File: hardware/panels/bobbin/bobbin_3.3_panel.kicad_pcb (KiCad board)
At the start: 2 copper layers, 68.5 x 105 mm, 34 parts

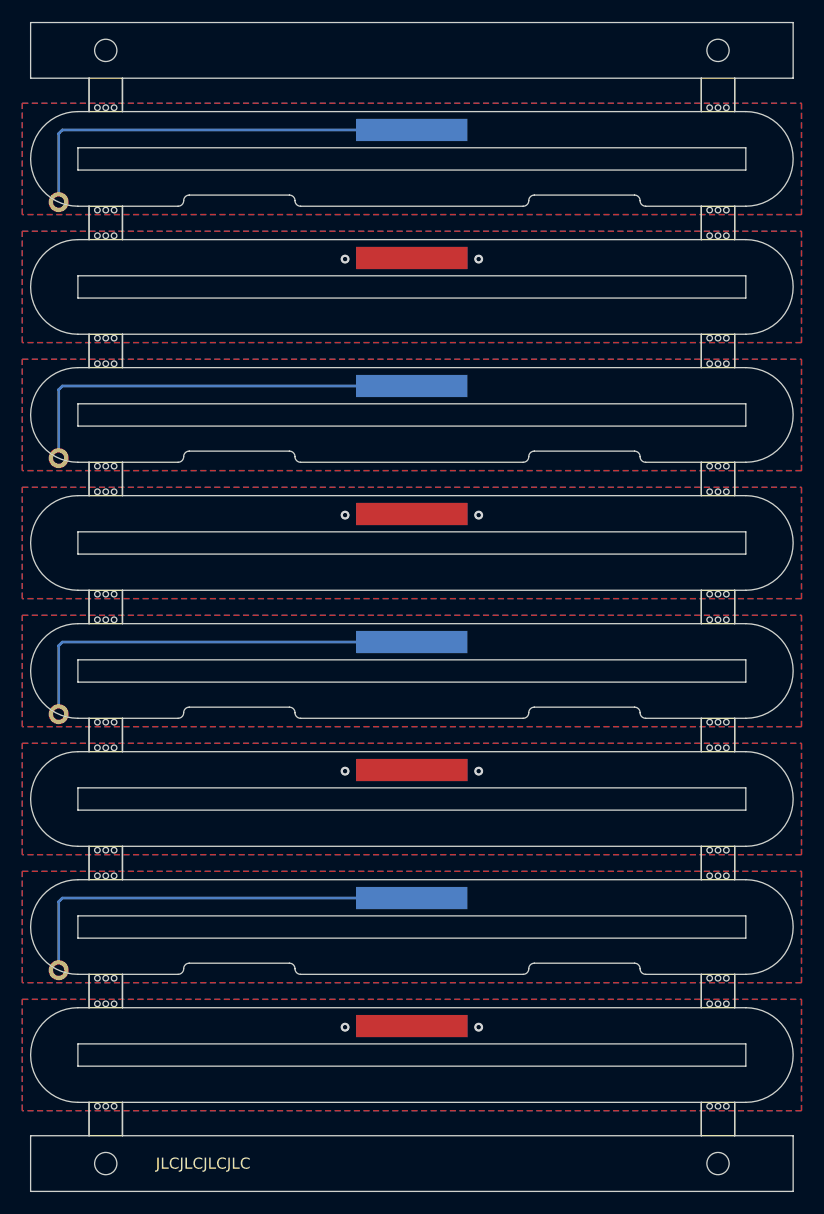
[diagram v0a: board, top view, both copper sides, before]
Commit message: Preamp, Tone Block, Passive, and Bobbin Panel updates
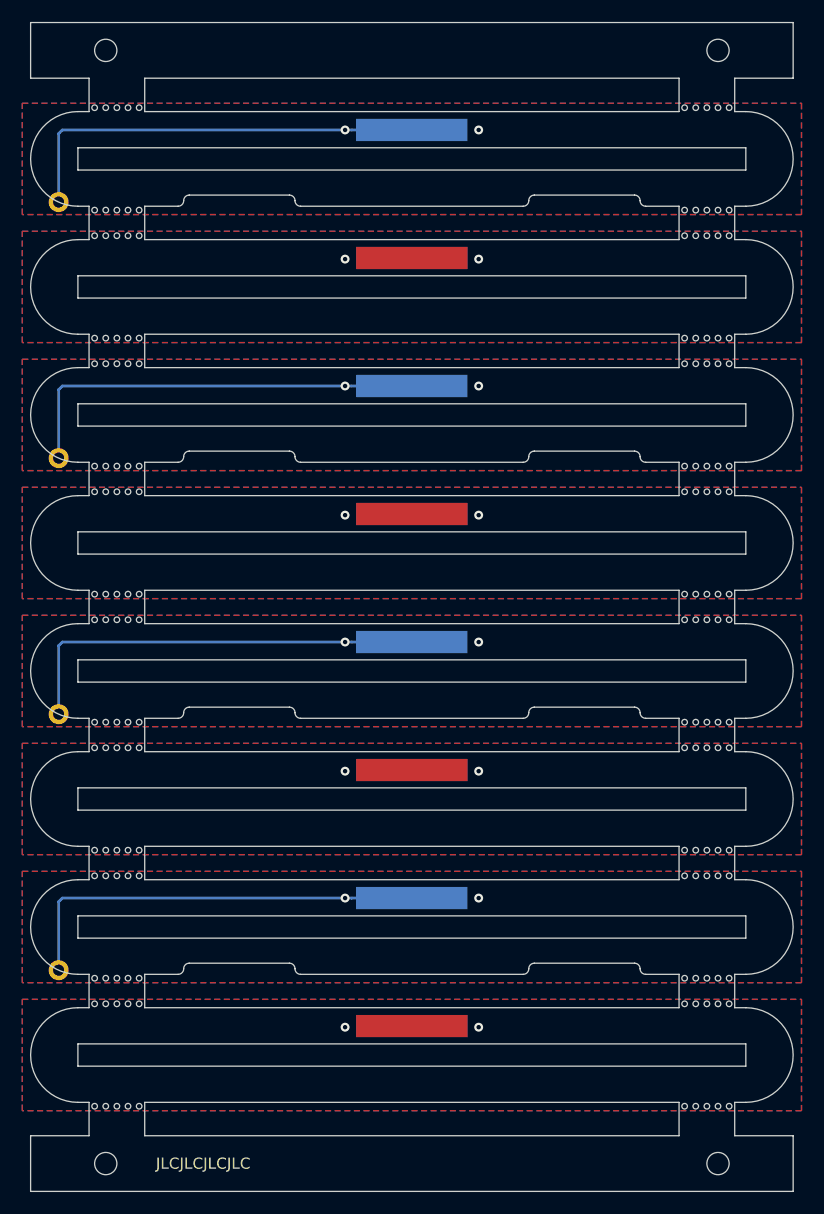
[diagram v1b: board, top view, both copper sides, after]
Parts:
- moved mouse-bite-3mm-slot 1.00 mm to (86.5, 116.5)
- moved mouse-bite-3mm-slot 1.00 mm to (86.5, 105.0)
- moved mouse-bite-3mm-slot 1.00 mm to (86.5, 82.0)
- moved mouse-bite-3mm-slot 1.00 mm to (86.5, 59.0)
- moved mouse-bite-3mm-slot 1.00 mm to (33.5, 93.5)
- moved mouse-bite-3mm-slot 1.00 mm to (33.5, 70.5)
- moved mouse-bite-3mm-slot 1.00 mm to (86.5, 47.5)
- moved mouse-bite-3mm-slot 1.00 mm to (33.5, 47.5)
- moved mouse-bite-3mm-slot 1.00 mm to (86.5, 36.0)
- moved mouse-bite-3mm-slot 1.00 mm to (33.5, 36.0)
- moved mouse-bite-3mm-slot 1.00 mm to (33.5, 116.5)
- moved mouse-bite-3mm-slot 1.00 mm to (86.5, 24.5)
- moved mouse-bite-3mm-slot 1.00 mm to (33.5, 24.5)
- moved mouse-bite-3mm-slot 1.00 mm to (33.5, 105.0)
- moved mouse-bite-3mm-slot 1.00 mm to (33.5, 82.0)
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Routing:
- net GND: vias 8 -> 16
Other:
- outline, holes or cut-outs redrawn
